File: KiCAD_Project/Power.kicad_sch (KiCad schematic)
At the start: 17 parts, among them J10 NP_Conn_01x02_Relief, J9 NP_Conn_01x02_Relief, Q1 1-0001670, U2 1-0000465, U3 1-0000576

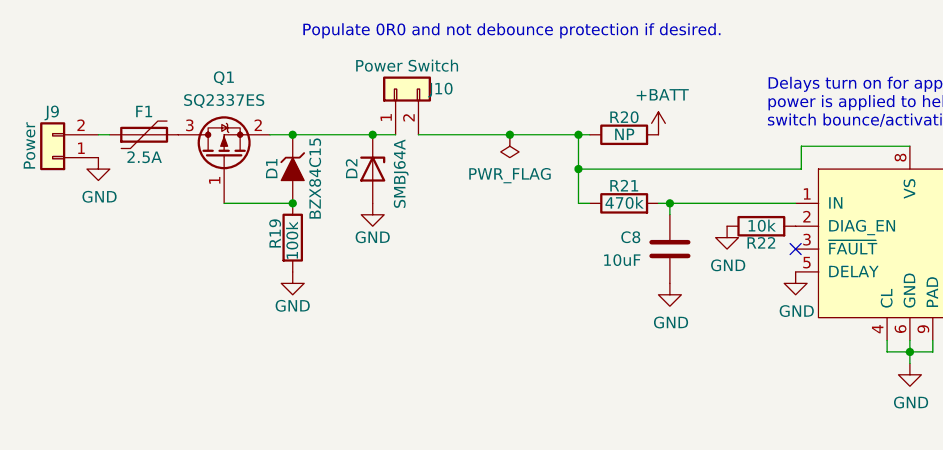
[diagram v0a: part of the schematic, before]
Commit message: Rev 2.1 Changes: - Fixed Issue #11 (U4 Footprint pin 1 indicator) - Added Open Log Header for breakout - Removed SD Circuit - Connected GPS to I2C - Updated IPN and Revision Number
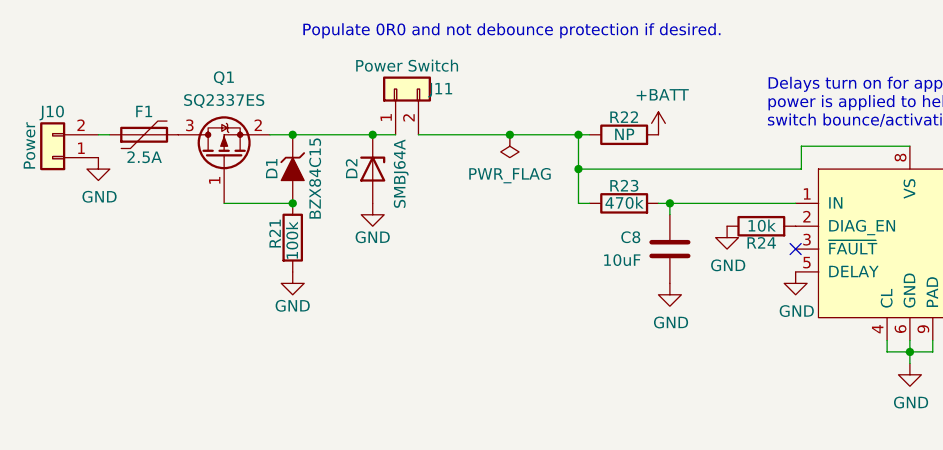
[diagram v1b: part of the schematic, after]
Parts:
- renumbered J9 to J10, J10 to J11, R19 to R21, R20 to R22, R21 to R23, R22 to R24
